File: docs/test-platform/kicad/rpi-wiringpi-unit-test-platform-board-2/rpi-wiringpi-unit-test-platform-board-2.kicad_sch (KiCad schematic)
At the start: 21 parts, among them J1 IN_PWR, J2 IN_SERVO, J3 IN_I2C, J4 IN_SPI, J5 IN_CS, J6 IN_SR, J7 Servo, M1 ADS1115_0x48, SW1 SW_DIP_x02, U1 74HC595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

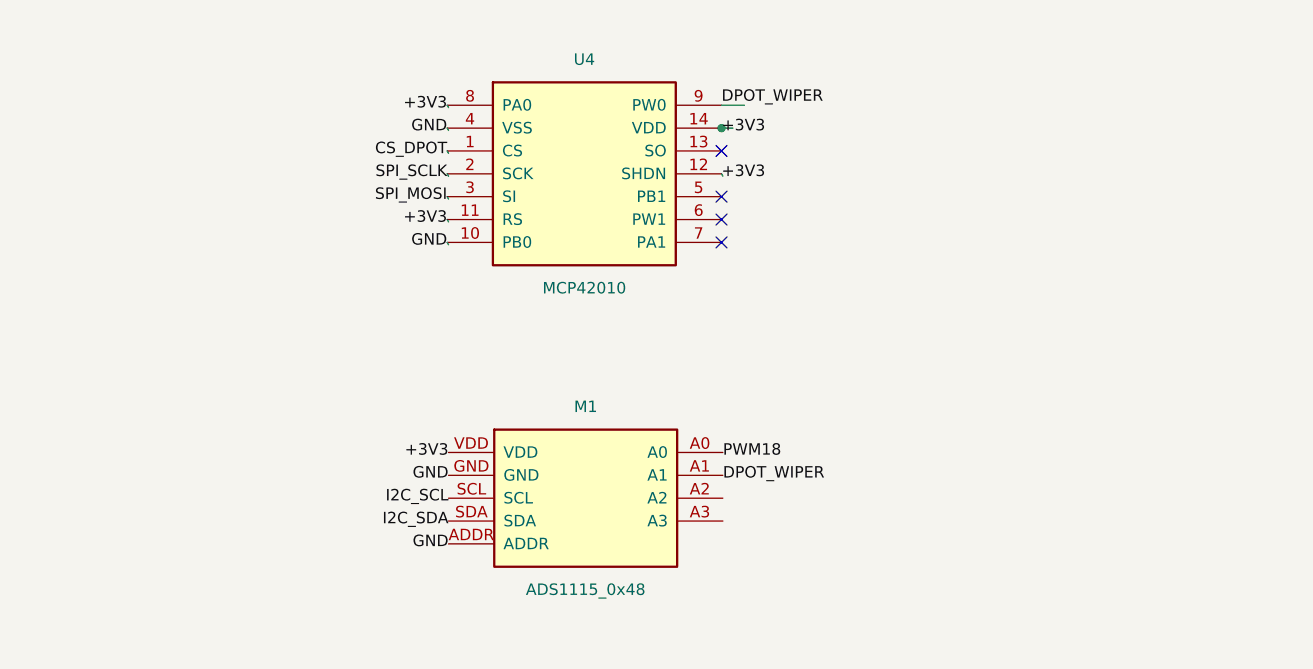
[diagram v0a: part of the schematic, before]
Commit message: Update dpot kicad files to enable pot 2
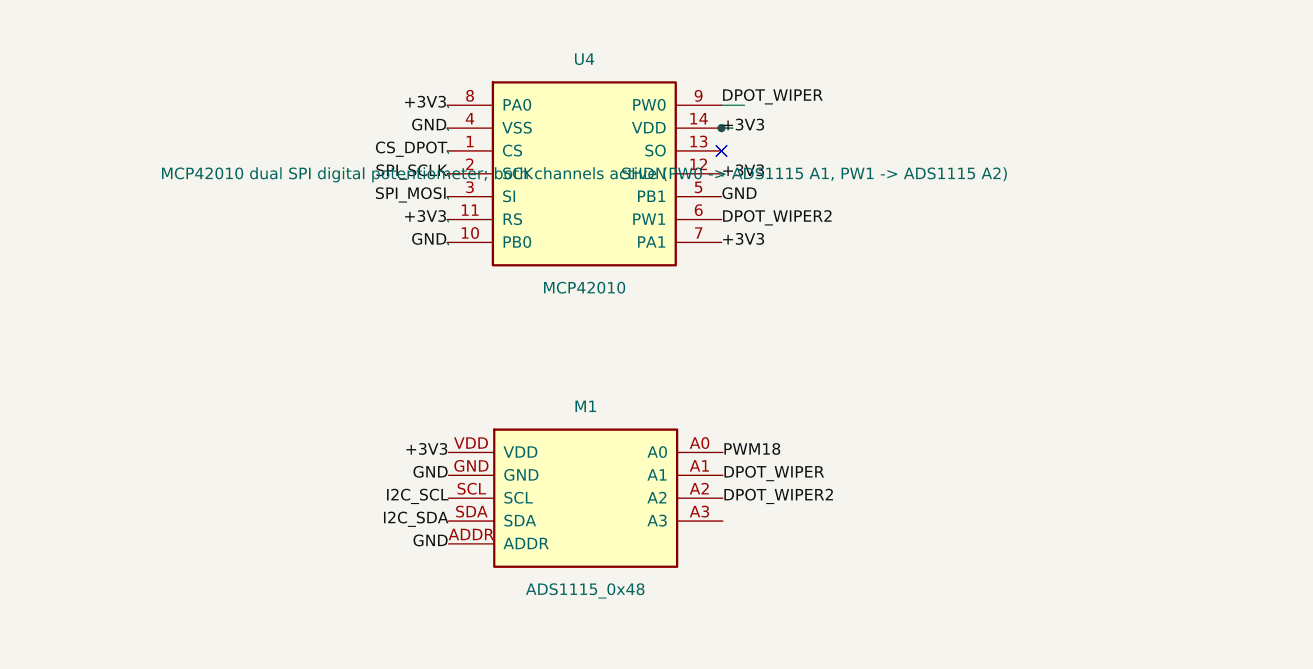
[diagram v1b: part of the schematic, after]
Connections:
- net +3V3: now also U4.7 (PA1)
- net GND: now also U4.5 (PB1)
- net DPOT_WIPER2: now reaches M1.A2
- net DPOT_WIPER2: now also U4.6 (PW1)
- no-connect marks 4 -> 1
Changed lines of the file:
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@@
 		(at 85.09 149.86)
-	)
-	(no_connect
-		(at 85.09 154.94)
-	)
-	(no_connect
-		(at 85.09 157.48)
-	)
-	(no_connect
-		(at 85.09 160.02)
 	)
 	(wire
@@
 			)
 			(justify left bottom)
+		)
+	)
+	(label "GND"
+		(at 85.09 154.94 0)
+		(effects
+			(font
+				(size 1.27 1.27)
+			)
+			(justify left)
+		)
+	)
+	(label "DPOT_WIPER2"
+		(at 85.09 157.48 0)
+		(effects
+			(font
+				(size 1.27 1.27)
+			)
+			(justify left)
+		)
+	)
+	(label "+3V3"
+		(at 85.09 160.02 0)
+		(effects
+			(font
+				(size 1.27 1.27)
+			)
+			(justify left)
+		)
+	)
+	(label "DPOT_WIPER2"
+		(at 85.24 188.44 0)
+		(effects
+			(font
+				(size 1.27 1.27)
+			)
+			(justify left)
 		)
 	)
@@
 			)
 		)
-		(property "Description" ""
+		(property "Description" "MCP42010 dual SPI digital potentiometer; both channels active (PW0 -> ADS1115 A1, PW1 -> ADS1115 A2)"
 			(at 69.85 152.4 0)
 			(show_name no)

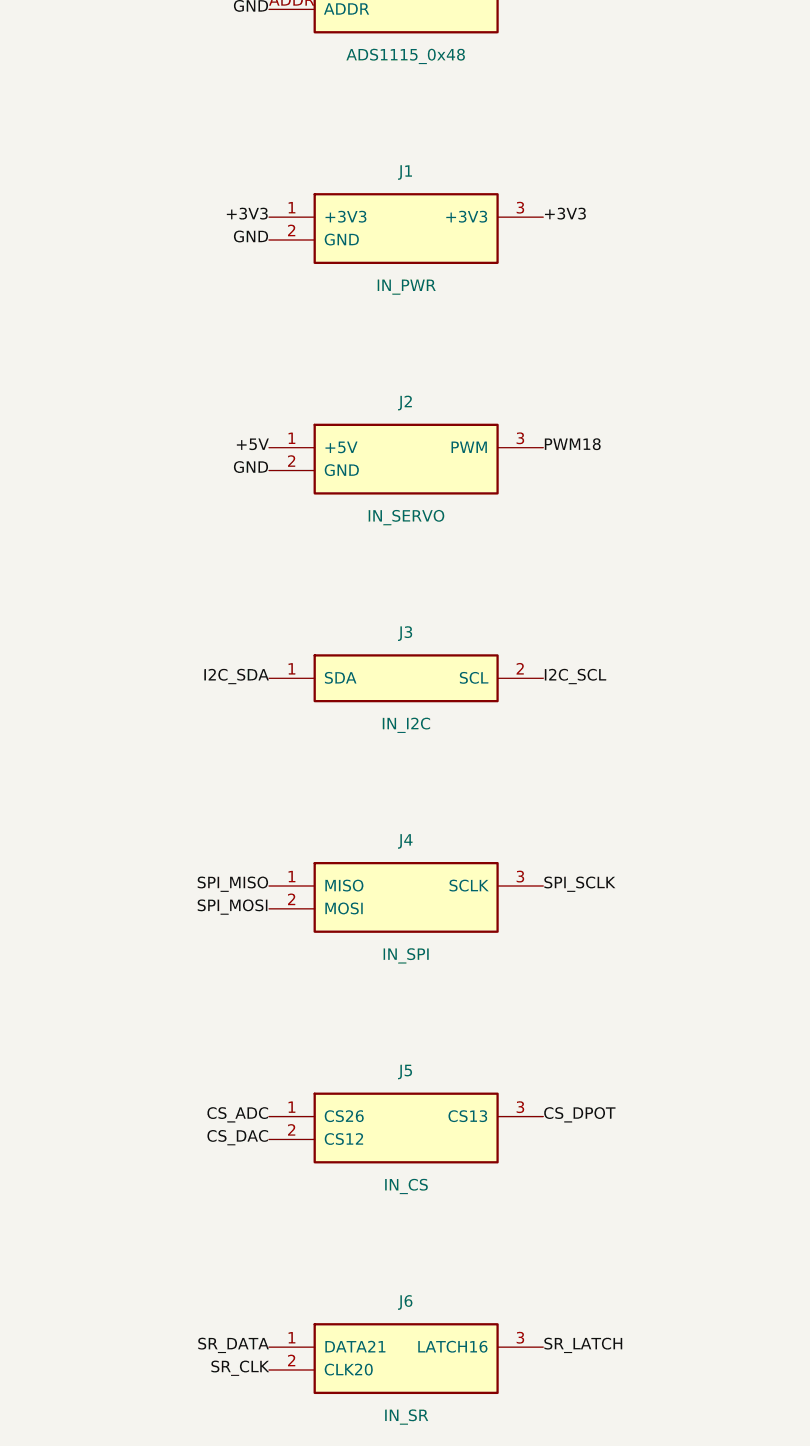
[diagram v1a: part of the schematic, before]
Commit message: Combined and merged Jx connectors
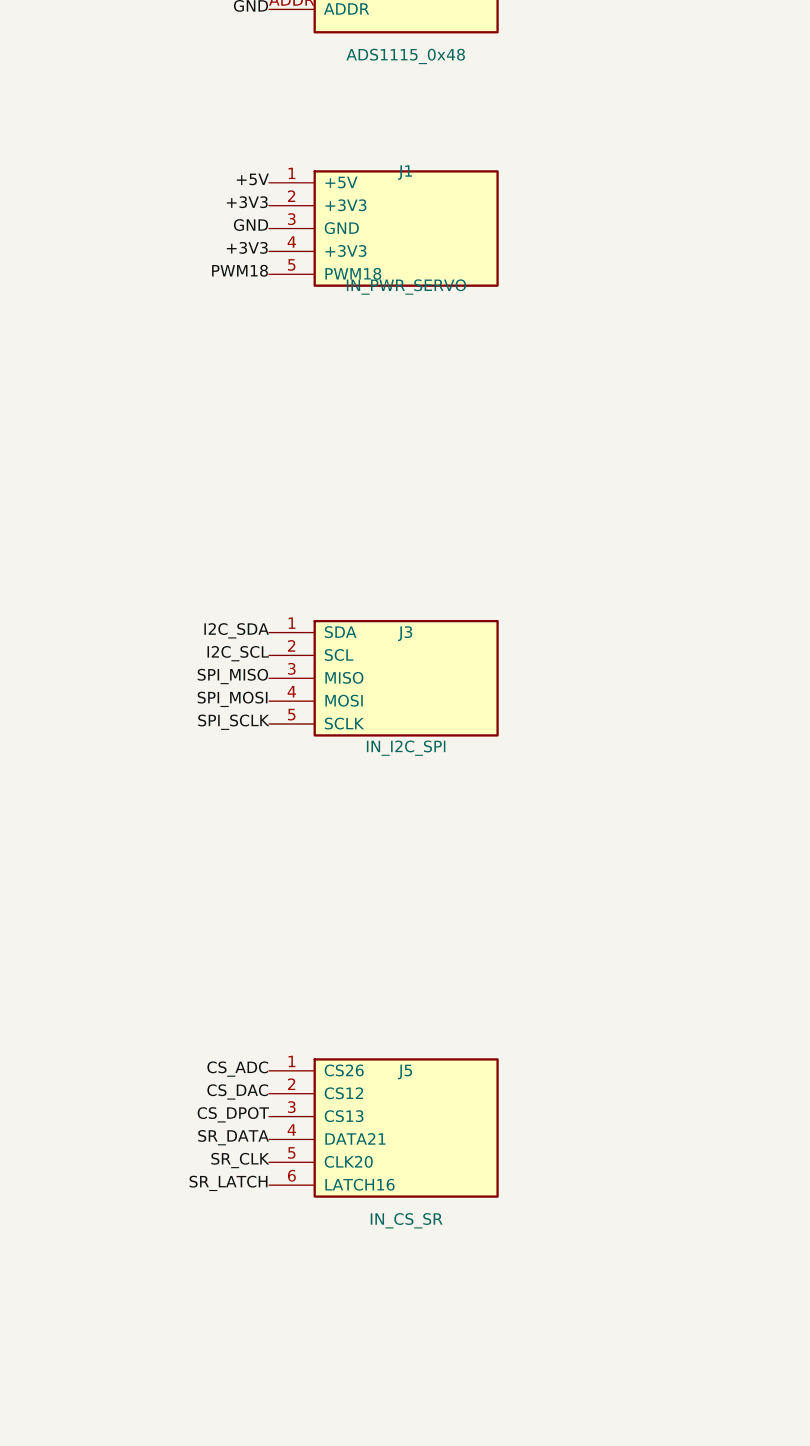
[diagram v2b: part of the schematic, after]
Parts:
- removed J2: IN_SERVO, rpi-wiringpi-unit-test-platform-board-2:J2, symbol rpi-wiringpi-unit-test-platform-board-2:J2
- removed J4: IN_SPI, rpi-wiringpi-unit-test-platform-board-2:J4, symbol rpi-wiringpi-unit-test-platform-board-2:J4
- removed J6: IN_SR, rpi-wiringpi-unit-test-platform-board-2:J6, symbol rpi-wiringpi-unit-test-platform-board-2:J6
- J1: value IN_PWR -> IN_PWR_SERVO
- J3: value IN_I2C -> IN_I2C_SPI
- J5: value IN_CS -> IN_CS_SR
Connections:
- net +3V3: now also J1.2 (+3V3), J1.4 (+3V3); no longer J1.1 (+3V3), J1.3 (+3V3)
- net +5V: now also J1.1 (+5V)
- net GND: now also J1.3 (GND); no longer J1.2 (GND)
- net PWM18: now also J1.5 (PWM18)
- net SPI_MISO: now also J3.3 (MISO)
- net SPI_MOSI: now also J3.4 (MOSI)
- net SPI_SCLK: now also J3.5 (SCLK)
- net SR_CLK: now also J5.5 (CLK20)
- net SR_DATA: now also J5.4 (DATA21)
- net SR_LATCH: now also J5.6 (LATCH16)
